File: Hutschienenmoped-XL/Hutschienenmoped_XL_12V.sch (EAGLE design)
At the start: 118 parts, among them J1 638207222005, J13 638207222005, J15 638207222008, J2 645004114822, J3 61302211821, J4 61300421121, J6 61302211821, J7 638207222005, J8 638207222007, U1 ESP32-S3-DEVKITC-1-N8R2, U4 TLE9250VSJ

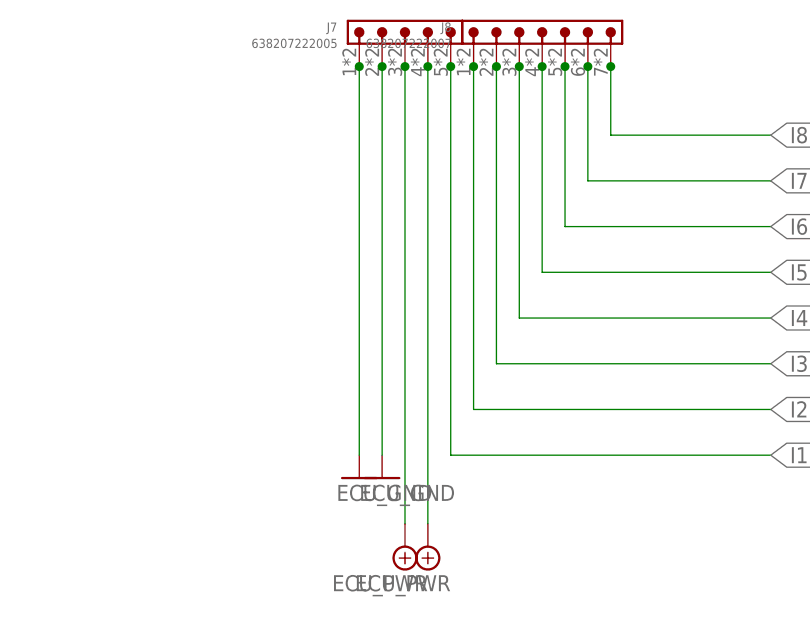
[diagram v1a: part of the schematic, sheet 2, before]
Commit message: Change grid unit to mm, adjust layer visibility and settings, update Fusion 360 sync status, modify wire connections and text positions.
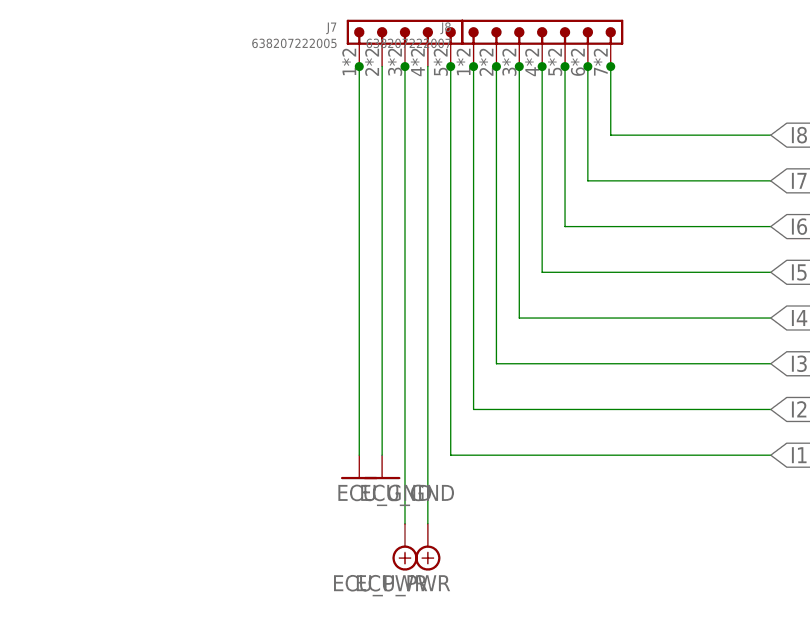
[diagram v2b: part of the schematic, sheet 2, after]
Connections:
- removed net N$16: J7.2
- removed net N$7: J7.4
- net ECU_GND: now also J7.2
- net ECU_PWR: now also J7.4
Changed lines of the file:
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@@
 <junction x="91.44" y="132.08"/>
+</segment>
+<segment>
+<pinref part="J7" gate="G$1" pin="4"/>
+<pinref part="ECU_PWR6" gate="ECU_PWR" pin="ECU_PWR"/>
+<wire x1="93.98" y1="132.08" x2="93.98" y2="81.28" width="0.1524" layer="91"/>
 </segment>
 </net>
@@
 <junction x="86.36" y="132.08"/>
 </segment>
-</net>
-<net name="N$7" class="0">
 <segment>
-<wire x1="93.98" y1="132.08" x2="93.98" y2="81.28" width="0.1524" layer="91"/>
-<pinref part="ECU_PWR6" gate="ECU_PWR" pin="ECU_PWR"/>
-<pinref part="J7" gate="G$1" pin="4"/>
-<junction x="93.98" y="132.08"/>
+<pinref part="ECU_GND26" gate="ECU_GND" pin="ECU_GND"/>
+<pinref part="J7" gate="G$1" pin="2"/>
+<wire x1="88.9" y1="88.9" x2="88.9" y2="132.08" width="0.1524" layer="91"/>
 </segment>
 </net>
-<net name="N$16" class="1">
-<segment>
-<wire x1="88.9" y1="132.08" x2="88.9" y2="88.9" width="0.1524" layer="91"/>
-<pinref part="ECU_GND26" gate="ECU_GND" pin="ECU_GND"/>
-<pinref part="J7" gate="G$1" pin="2"/>
-<junction x="88.9" y="132.08"/>
-</segment>
-</net>

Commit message: NOT correct !
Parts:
- removed J3, J6: 61302211821, Wurth_Connectors_WR-PHD:6130XX11821_61302211821
- removed U1: ESP32-S3-DEVKITC-1-N8R2, ESP32-S3-DEVKITC-1-N8R2:ESP32-S3-DEVKITC-1-N8R2
- added ESP32-J1, ESP32-J3: 61302211821, Wurth_Connectors_WR-PHD:6130XX11821_61302211821
- added MP1, MP2, MP3, MP4, MP5, MP6, MP7, MP8: M3 x 2.5mm, Wurth_Assembly_WA-SMSI:WA-SMSI_9774XXX360_9774025360R
- added R14, R15: 13K, resistor:R-EU_R1206
- added W1-J1, W2-J1: 61301015721, WE-special:6130XX15721_61301015721
- added W1-J2, W2-J2: 61300615721, Wurth_Connectors_WR-PHD:6130XX15721_61300615721
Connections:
- removed net IX00: U1.GPIO14
- removed net IX06: U1.GPIO15
- removed net MB_UART_RTS1: U1.GPIO10
- removed net MB_UART_RXD1: U1.GPIO8
- removed net MB_UART_RXD2: U1.GPIO11
- removed net N$20: J13.5
- removed net QX06: U1.GPIO48
- removed net QX07: U1.GPIO38
- new net CS0: ESP32-J1.14, W1-J1.6
- new net CS1: ESP32-J1.12, W2-J1.6
- new net INT0: ESP32-J3.16, W1-J2.5
- new net INT1: ESP32-J3.15, W2-J2.5
- new net MISO: ESP32-J1.20, W1-J1.4, W2-J1.4
- new net MOSI: ESP32-J1.17, W1-J1.3, W2-J1.3
- new net RST0: ESP32-J1.9, W1-J2.3
- new net RST1: ESP32-J3.10, W2-J2.3
- new net SCLK: ESP32-J1.16, W1-J1.5, W2-J1.5
- net +3V3: now also ESP32-J1.1, ESP32-J1.2, W1-J1.7, W1-J1.8, W1-J2.1, W2-J1.7, W2-J1.8, W2-J2.1; no longer U1.3V3
- net +5V: now also ESP32-J1.21; no longer U1.5V0
- net BOOT: now also ESP32-J3.14; no longer U1.GPIO0
- net CAN1_RXD: now also ESP32-J1.5; no longer U1.GPIO5
- net CAN1_TXD: now also ESP32-J1.4; no longer U1.GPIO4
- net CI1: now also ESP32-J1.19; no longer U1.GPIO13
- net CI2: now also ESP32-J1.18; no longer U1.GPIO12
- net CI3: now also ESP32-J1.15; no longer U1.GPIO9
- net CI4: now also ESP32-J1.13; no longer U1.GPIO3
- net CI5: now also ESP32-J1.11; no longer U1.GPIO18
- net CI6: now also ESP32-J1.10; no longer U1.GPIO17
- net CI7: now also ESP32-J1.7; no longer U1.GPIO7
- net CI8: now also ESP32-J1.6; no longer U1.GPIO6
- net ECU_GND: now also ESP32-J1.22, ESP32-J3.1, ESP32-J3.21, ESP32-J3.22, MP5.1, MP6.1, MP7.1, MP8.1, R14.1, R15.1, W1-J1.1, W1-J1.2, W1-J2.6, W2-J1.1, W2-J1.2, W2-J2.6; no longer U1.GND
- net PWR_GND: now also J13.5, MP1.1, MP2.1, MP3.1, MP4.1
- net Q1C: now also ESP32-J3.18; no longer U1.GPIO21
- net Q2C: now also ESP32-J3.17, R15.2; no longer U1.GPIO47
- net Q3C: now also ESP32-J3.9, R14.2; no longer U1.MTCK/GPIO39
- net Q4C: now also ESP32-J3.8; no longer U1.MTDO/GPIO40
- net Q5C: now also ESP32-J3.7; no longer U1.MTDI/GPIO41
- net Q6C: now also ESP32-J3.6; no longer U1.MTMS/GPIO42
- net Q7C: now also ESP32-J3.4; no longer U1.GPIO1
- net Q8C: now also ESP32-J3.5; no longer U1.GPIO2
- net RESET: now also ESP32-J1.3; no longer U1.RST
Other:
- note added: "prg"
- note added: "psram"
- note added: "usb"

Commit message: Update grid distance to 70mm, layer visibility adjustments.
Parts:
- removed MP1, MP2, MP3, MP4, MP5, MP6, MP7, MP8: M3 x 2.5mm, Wurth_Assembly_WA-SMSI:WA-SMSI_9774XXX360_9774025360R
- removed W1-J1, W2-J1: 61301015721, WE-special:6130XX15721_61301015721
- removed W1-J2, W2-J2: 61300615721, Wurth_Connectors_WR-PHD:6130XX15721_61300615721
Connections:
- net +3V3: no longer W1-J1.7, W1-J1.8, W1-J2.1, W2-J1.7, W2-J1.8, W2-J2.1
- net CS0: no longer W1-J1.6
- net CS1: no longer W2-J1.6
- net ECU_GND: no longer MP5.1, MP6.1, MP7.1, MP8.1, W1-J1.1, W1-J1.2, W1-J2.6, W2-J1.1, W2-J1.2, W2-J2.6
- net INT0: no longer W1-J2.5
- net INT1: no longer W2-J2.5
- net MISO: no longer W1-J1.4, W2-J1.4
- net MOSI: no longer W1-J1.3, W2-J1.3
- net PWR_GND: no longer MP1.1, MP2.1, MP3.1, MP4.1
- net RST0: no longer W1-J2.3
- net RST1: no longer W2-J2.3
- net SCLK: no longer W1-J1.5, W2-J1.5

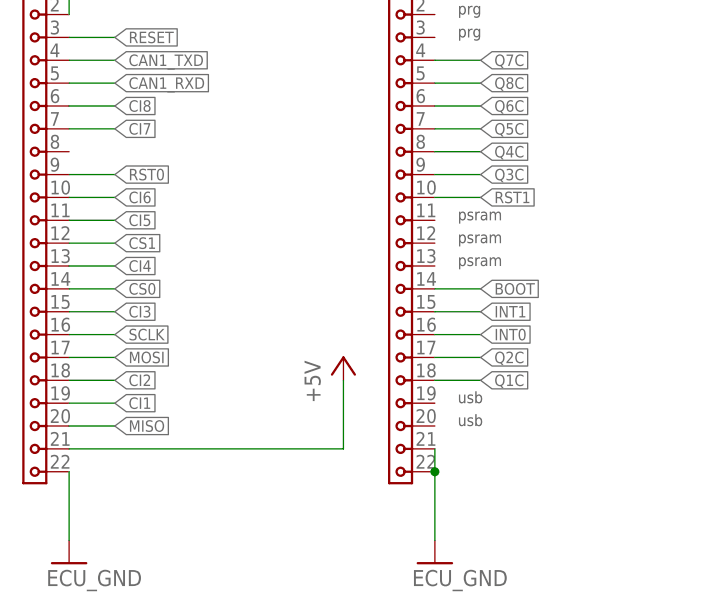
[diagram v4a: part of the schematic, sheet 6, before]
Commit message: Update grid settings and Fusion 360 sync details, remove redundant wires and text elements, optimize polygon vertices, clean up vias and wire connections.
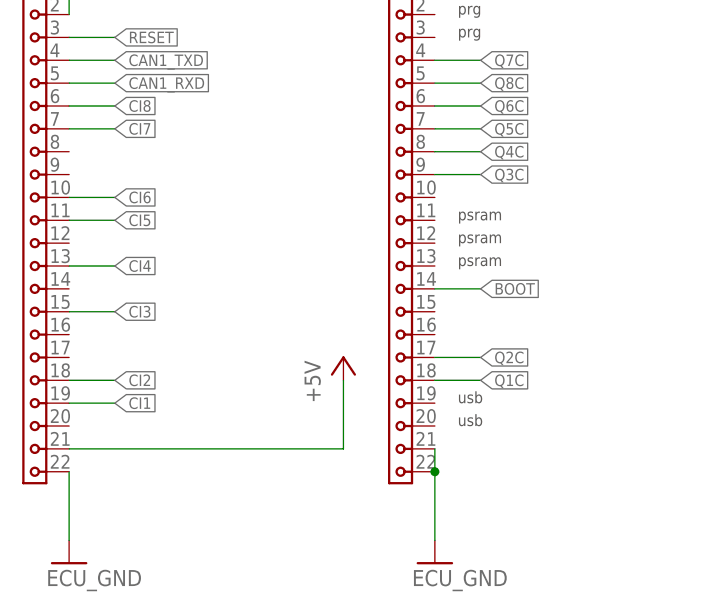
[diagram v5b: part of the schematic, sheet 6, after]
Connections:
- removed net CS0: ESP32-J1.14
- removed net CS1: ESP32-J1.12
- removed net INT0: ESP32-J3.16
- removed net INT1: ESP32-J3.15
- removed net MISO: ESP32-J1.20
- removed net MOSI: ESP32-J1.17
- removed net RST0: ESP32-J1.9
- removed net RST1: ESP32-J3.10
- removed net SCLK: ESP32-J1.16
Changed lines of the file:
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@@
-</segment>
-</net>
-<net name="RST1" class="0">
-<segment>
-<pinref part="ESP32-J3" gate="G$1" pin="10"/>
-<wire x1="144.78" y1="106.68" x2="149.86" y2="106.68" width="0.1524" layer="91"/>
-<label x="149.86" y="106.68" size="1.27" layer="95" xref="yes"/>
-</segment>
-</net>
-<net name="INT1" class="0">
-<segment>
-<pinref part="ESP32-J3" gate="G$1" pin="15"/>
-<wire x1="144.78" y1="93.98" x2="149.86" y2="93.98" width="0.1524" layer="91"/>
-<label x="149.86" y="93.98" size="1.27" layer="95" xref="yes"/>
-</segment>
-</net>
-<net name="INT0" class="0">
-<segment>
-<pinref part="ESP32-J3" gate="G$1" pin="16"/>
-<wire x1="144.78" y1="91.44" x2="149.86" y2="91.44" width="0.1524" layer="91"/>
-<label x="149.86" y="91.44" size="1.27" layer="95" xref="yes"/>
-</segment>
-</net>
-<net name="MISO" class="0">
-<segment>
-<pinref part="ESP32-J1" gate="G$1" pin="20"/>
-<wire x1="104.14" y1="81.28" x2="109.22" y2="81.28" width="0.1524" layer="91"/>
-<label x="109.22" y="81.28" size="1.27" layer="95" xref="yes"/>
-</segment>
-</net>
-<net name="MOSI" class="0">
-<segment>
-<pinref part="ESP32-J1" gate="G$1" pin="17"/>
-<wire x1="104.14" y1="88.9" x2="109.22" y2="88.9" width="0.1524" layer="91"/>
-<label x="109.22" y="88.9" size="1.27" layer="95" xref="yes"/>
-</segment>
-</net>
-<net name="SCLK" class="0">
-<segment>
-<pinref part="ESP32-J1" gate="G$1" pin="16"/>
-<wire x1="104.14" y1="91.44" x2="109.22" y2="91.44" width="0.1524" layer="91"/>
-<label x="109.22" y="91.44" size="1.27" layer="95" xref="yes"/>
-</segment>
-</net>
-<net name="CS0" class="0">
-<segment>
-<pinref part="ESP32-J1" gate="G$1" pin="14"/>
-<wire x1="104.14" y1="96.52" x2="109.22" y2="96.52" width="0.1524" layer="91"/>
-<label x="109.22" y="96.52" size="1.27" layer="95" xref="yes"/>
-</segment>
-</net>
-<net name="CS1" class="0">
-<segment>
-<pinref part="ESP32-J1" gate="G$1" pin="12"/>
-<wire x1="104.14" y1="101.6" x2="109.22" y2="101.6" width="0.1524" layer="91"/>
-<label x="109.22" y="101.6" size="1.27" layer="95" xref="yes"/>
-</segment>
-</net>
-<net name="RST0" class="0">
-<segment>
-<pinref part="ESP32-J1" gate="G$1" pin="9"/>
-<wire x1="104.14" y1="109.22" x2="109.22" y2="109.22" width="0.1524" layer="91"/>
-<label x="109.22" y="109.22" size="1.27" layer="95" xref="yes"/>
 </segment>
 </net>

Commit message: not good !
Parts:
- added R16, R17, R19, R20, R33, R34: 13K, resistor:R-EU_R1206
- added RESET: (no value), Wurth_Switch_WS-TATU:431256083736
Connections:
- net ECU_GND: now also R16.1, R17.1, R19.1, R20.1, R33.1, R34.1, RESET.2, RESET.GND, RESET.GND1
- net Q1C: now also R33.2
- net Q4C: now also R16.2
- net Q5C: now also R17.2
- net Q6C: now also R19.2
- net Q7C: now also R20.2
- net Q8C: now also R34.2
- net RESET: now also RESET.3
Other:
- moved on the sheet: R14, R15
